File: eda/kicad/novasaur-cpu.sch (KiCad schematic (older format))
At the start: 29 parts, among them U14 27C020, U15 AS6C4008, U16 74F574, U17 74F163, U18 74F163, U19 74F541, U20 74F574, U21 74F574, U22 74F257, U23 74F574, U24 74F574, U25 74F574, U26 74F574, U27 74F244, U27 74F541

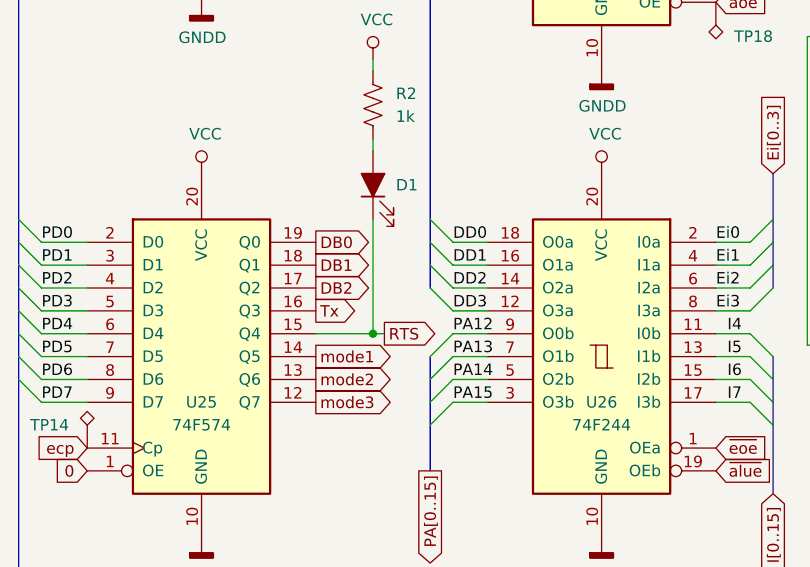
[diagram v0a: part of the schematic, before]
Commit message: build out, fix bugs Build out the initial HAL VM code to generate video timing. Not quite working yet, but lots of bugs fixed with assembler and code
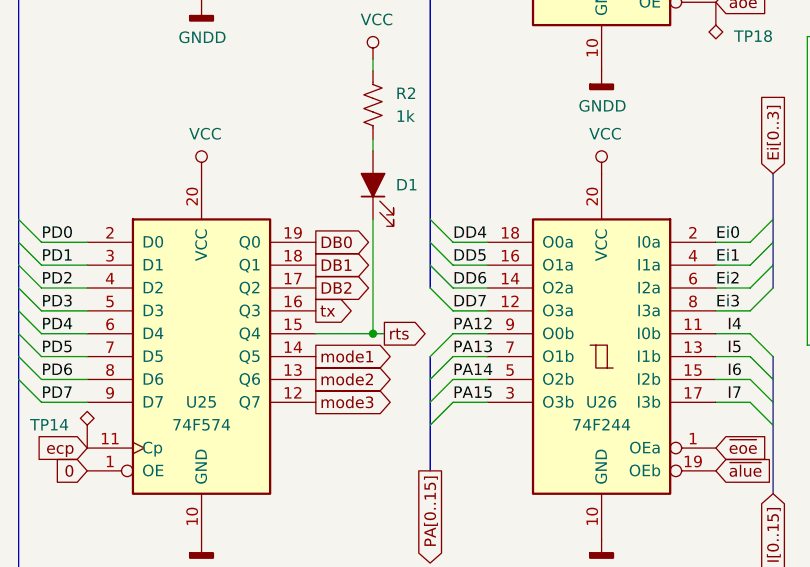
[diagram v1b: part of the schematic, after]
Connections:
- net DD0: no longer U27.18 (O0a)
- net DD1: no longer U27.16 (O1a)
- net DD2: no longer U27.14 (O2a)
- net DD3: no longer U27.12 (O3a)
- net DD4: now also U27.18 (O0a)
- net DD5: now also U27.16 (O1a)
- net DD6: now also U27.14 (O2a)
- net DD7: now also U27.12 (O3a)
- net RTS renamed rts
- net Tx renamed tx
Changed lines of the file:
@@
 Sheet 2 4
 Title "CPU"
-Date "2020-02-15"
+Date "2020-02-20"
 Rev "1.5"
 Comp ""
@@
 PA12
 Text Label 2650 6350 0    50   ~ 0
-DD3
+DD7
 Text Label 2650 6250 0    50   ~ 0
-DD2
+DD6
 Text Label 2650 6150 0    50   ~ 0
-DD1
+DD5
 Text Label 2650 6050 0    50   ~ 0
-DD0
+DD4
 Wire Wire Line
 	2650 6050 2800 6050
@@
 FD[0..7]
 Text GLabel 2050 6350 2    50   Output ~ 0
-Tx
+tx
 Text GLabel 2350 6450 2    50   Output ~ 0
-RTS
+rts
 Text GLabel 2050 6550 2    50   Output ~ 0
 mode1

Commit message: rename P reg to T
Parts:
- TP15: value ~POE -> ~TOE
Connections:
- net ~poe renamed ~toe
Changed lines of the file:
@@
 Sheet 2 4
 Title "CPU"
-Date "2020-03-08"
+Date "2020-03-29"
 Rev "1.6"
 Comp ""
@@
 PD[0..7]
 Text GLabel 4250 2400 0    50   Input ~ 0
-~poe
+~toe
 $Comp
 L 74xx:74LS574 U?
@@
 AR Path="/5DA1E9BD/5E39EF69" Ref="TP?"  Part="1"
 F 0 "TP15" H 4300 2550 50  0000 L CNN
-F 1 "~POE" H 4000 2550 50  0001 L CNN
+F 1 "~TOE" H 4000 2550 50  0001 L CNN
 F 2 "TestPoint:TestPoint_Pad_1.0x1.0mm" H 4450 2400 50  0001 C CNN
 F 3 "~" H 4450 2400 50  0001 C CNN

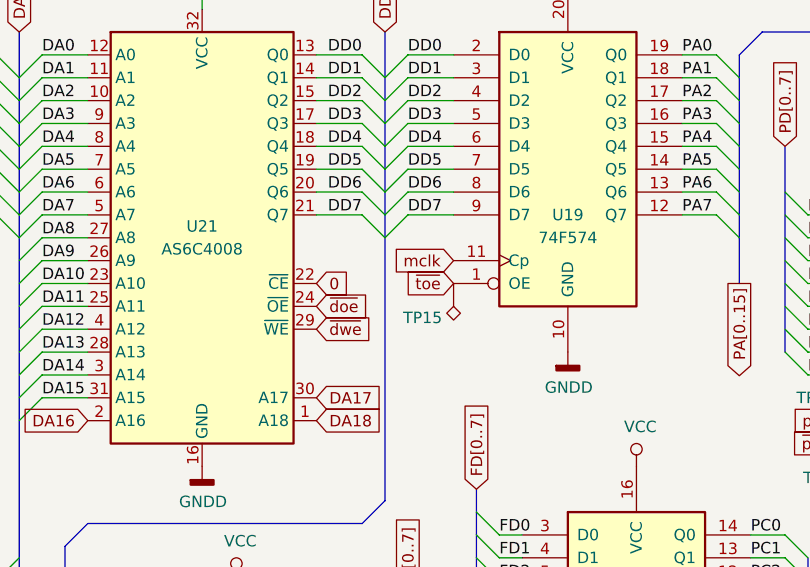
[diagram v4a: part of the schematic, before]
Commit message: add video headers
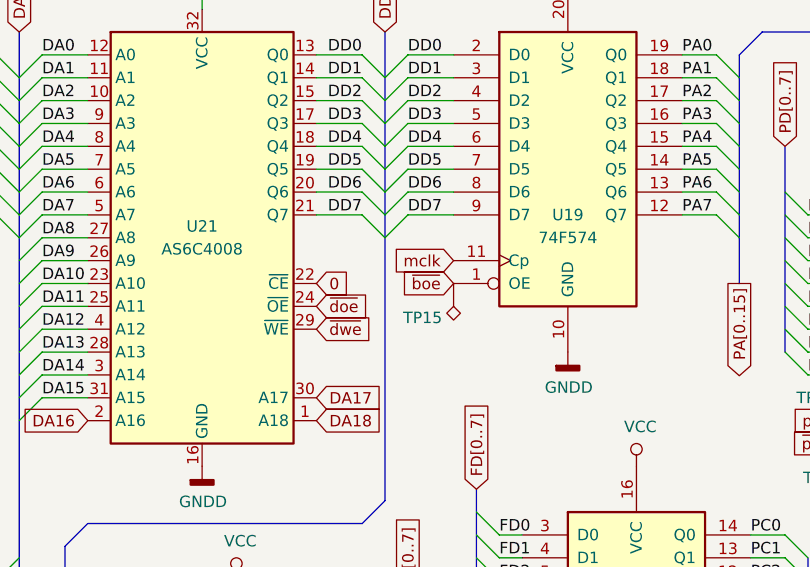
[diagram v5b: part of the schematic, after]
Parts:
- TP15: value ~TOE -> ~BOE
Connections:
- net ~toe renamed ~boe
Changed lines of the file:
@@
 encoding utf-8
 Sheet 2 4
-Title "CPU"
-Date "2020-03-29"
+Title "Novasaur Retrocomputer"
+Date "2020-03-31"
 Rev "1.6"
 Comp ""
@@
 PD[0..7]
 Text GLabel 4250 2400 0    50   Input ~ 0
-~toe
+~boe
 $Comp
 L 74xx:74LS574 U?
@@
 AR Path="/5DA1E9BD/5E39EF69" Ref="TP?"  Part="1"
 F 0 "TP15" H 4300 2550 50  0000 L CNN
-F 1 "~TOE" H 4000 2550 50  0001 L CNN
+F 1 "~BOE" H 4000 2550 50  0001 L CNN
 F 2 "TestPoint:TestPoint_Pad_1.0x1.0mm" H 4450 2400 50  0001 C CNN
 F 3 "~" H 4450 2400 50  0001 C CNN

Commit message: power sw + super caps
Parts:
- renumbered R2 to R1
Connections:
- net 0: no longer U15.22 (~CE)
- net VCC: no longer U15.32 (VCC)
- net I4 renamed C4
- net I5 renamed C5
- net I6 renamed C6
- net I7 renamed C7
- new net +BATT: U15.32 (VCC)
- new net ~dce: U15.22 (~CE)
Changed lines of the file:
@@
 Sheet 2 4
 Title "Novasaur Retrocomputer"
-Date "2020-03-31"
+Date "2020-05-02"
 Rev "1.6"
 Comp ""
@@
 Ei3
 Text Label 3850 6650 0    50   ~ 0
-I6
+C6
 Text Label 3850 6550 0    50   ~ 0
-I5
+C5
 Text Label 3850 6450 0    50   ~ 0
-I4
+C4
 Text Label 3850 6750 0    50   ~ 0
-I7
+C7
 Wire Wire Line
 	10000 5250 10150 5250
@@
 L power:VCC #PWR?
 U 1 1 5DAE3651
-P 8100 1200
+P 8100 1100
 AR Path="/5F6C0B36/5DAE3651" Ref="#PWR?"  Part="1"
 AR Path="/5DAA19D5/5DAE3651" Ref="#PWR0169"  Part="1"
 AR Path="/5DAA5CD8/5D99DA9F/5DAE3651" Ref="#PWR?"  Part="1"
 AR Path="/5DA1E9BA/5DAE3651" Ref="#PWR0129"  Part="1"
-F 0 "#PWR0129" H 8100 1050 50  0001 C CNN
-F 1 "VCC" H 8117 1373 50  0000 C CNN
-F 2 "" H 8100 1200 50  0001 C CNN
-F 3 "" H 8100 1200 50  0001 C CNN
-	1    8100 1200
+F 0 "#PWR0129" H 8100 950 50  0001 C CNN
+F 1 "VCC" H 8117 1273 50  0000 C CNN
+F 2 "" H 8100 1100 50  0001 C CNN
+F 3 "" H 8100 1100 50  0001 C CNN
+	1    8100 1100
 	1    0    0    -1
 $EndComp
@@
 $EndComp
 Wire Wire Line
-	3150 1200 3150 1100
-$Comp
-L power:VCC #PWR?
-U 1 1 5DAE363F
-P 3150 1100
-AR Path="/5F6C0B36/5DAE363F" Ref="#PWR?"  Part="1"
-AR Path="/5DAA19D5/5DAE363F" Ref="#PWR0166"  Part="1"
-AR Path="/5DAA5CD8/5D99DA9F/5DAE363F" Ref="#PWR?"  Part="1"
-AR Path="/5DA1E9BA/5DAE363F" Ref="#PWR0142"  Part="1"
-F 0 "#PWR0142" H 3150 950 50  0001 C CNN
-F 1 "VCC" H 3167 1273 50  0000 C CNN
-F 2 "" H 3150 1100 50  0001 C CNN
-F 3 "" H 3150 1100 50  0001 C CNN
-	1    3150 1100
-	1    0    0    -1
-$EndComp
-Wire Wire Line
 	2450 1400 2650 1400
 Wire Wire Line
@@
 	2450 2900 2650 2900
 Text GLabel 4050 7150 3    50   Input ~ 0
-I[0..15]
+C[0..15]
 Text GLabel 3950 1300 1    50   Input ~ 0
 DD[0..7]
@@
 DA17
 Text GLabel 3650 2400 2    50   Input ~ 0
-0
+~dce
 Text GLabel 3650 2600 2    50   Input ~ 0
 ~dwe
@@
 AR Path="/5DA1E9BA/5EE6CB39" Ref="D1"  Part="1"
 AR Path="/5EE6CB39" Ref="D?"  Part="1"
-F 0 "D1" V 2300 5700 50  0000 R CNN
+F 0 "D1" V 2300 6000 50  0000 R CNN
 F 1 "4300H1LC" V 2248 5683 50  0001 R CNN
 F 2 "LED_THT:LED_D5.0mm_Horizontal_O1.27mm_Z3.0mm" H 2300 5800 50  0001 C CNN
@@
 AR Path="/5DAA19D5/5EE6CB33" Ref="R?"  Part="1"
 AR Path="/5DAA5CD8/5D99DA9F/5EE6CB33" Ref="R?"  Part="1"
-AR Path="/5DA1E9BA/5EE6CB33" Ref="R2"  Part="1"
+AR Path="/5DA1E9BA/5EE6CB33" Ref="R1"  Part="1"
 AR Path="/5EE6CB33" Ref="R?"  Part="1"
-F 0 "R2" H 2400 5500 50  0000 L CNN
-F 1 "1k" H 2400 5400 50  0000 L CNN
+F 0 "R1" H 2100 5500 50  0000 L CNN
+F 1 "1k" H 2100 5400 50  0000 L CNN
 F 2 "Resistor_THT:R_Axial_DIN0204_L3.6mm_D1.6mm_P7.62mm_Horizontal" V 2340 5440 50  0001 C CNN
 F 3 "~" H 2300 5450 50  0001 C CNN
@@
 Wire Wire Line
 	2300 5650 2300 5600
+$Comp
+L power:+BATT #PWR0142
+U 1 1 5EC0EA23
+P 3150 1100
+F 0 "#PWR0142" H 3150 950 50  0001 C CNN
+F 1 "+BATT" H 3165 1273 50  0000 C CNN
+F 2 "" H 3150 1100 50  0001 C CNN
+F 3 "" H 3150 1100 50  0001 C CNN
+	1    3150 1100
+	1    0    0    -1
+$EndComp
+Wire Wire Line
+	3150 1200 3150 1100
+Wire Wire Line
+	8100 1200 8100 1100
 Wire Bus Line
 	4350 3300 4350 3700

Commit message: update serial
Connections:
- net Ei0 renamed rx
- net Ei1 renamed cts
- net Ei2 renamed ps2clk
- net Ei3 renamed ps2rx
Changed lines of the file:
@@
 encoding utf-8
 Sheet 2 4
-Title "Novasaur Retrocomputer"
-Date "2020-05-02"
+Title "Central Processing Unit"
+Date "2020-05-24"
 Rev "1.6"
 Comp ""
@@
 Wire Wire Line
 	3800 6450 3950 6450
-Wire Wire Line
-	3800 6350 3950 6350
-Wire Wire Line
-	3800 6150 3950 6150
-Wire Wire Line
-	3800 6050 3950 6050
 Entry Wire Line
 	3950 6750 4050 6850
@@
 Entry Wire Line
 	3950 6450 4050 6550
-Entry Wire Line
-	3950 6050 4050 5950
-Entry Wire Line
-	3950 6150 4050 6050
-Entry Wire Line
-	3950 6250 4050 6150
-Entry Wire Line
-	3950 6350 4050 6250
 Text Label 2650 6750 0    50   ~ 0
 PA15
@@
 Entry Wire Line
 	2550 6850 2650 6750
-Wire Wire Line
-	3950 6250 3800 6250
-Text Label 3800 6050 0    50   ~ 0
-Ei0
-Text Label 3800 6150 0    50   ~ 0
-Ei1
-Text Label 3800 6250 0    50   ~ 0
-Ei2
-Text Label 3800 6350 0    50   ~ 0
-Ei3
 Text Label 3850 6650 0    50   ~ 0
 C6
@@
 Text GLabel 4350 5600 1    50   Input ~ 0
 FD[0..7]
-Text GLabel 4050 5750 1    50   Input ~ 0
-Ei[0..3]
 Wire Wire Line
 	8900 4850 8900 4650
@@
 Wire Wire Line
 	8100 1200 8100 1100
+Text GLabel 3800 6050 2    50   Input ~ 0
+rx
+Text GLabel 3800 6150 2    50   Input ~ 0
+cts
+Text GLabel 3800 6250 2    50   Input ~ 0
+ps2clk
+Text GLabel 3800 6350 2    50   Input ~ 0
+ps2rx
 Wire Bus Line
 	4350 3300 4350 3700
@@
 	2550 6550 2550 7050
 Wire Bus Line
-	4050 5750 4050 6250
-Wire Bus Line
 	4050 6550 4050 7150

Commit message: checkin work in progress on video timing
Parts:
- D1: value 4300H1LC -> LTL-10223W
- R1: value 1k -> 330
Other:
- moved on the sheet: TP19, TP20, U16
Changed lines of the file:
@@
 Sheet 2 4
 Title "Central Processing Unit"
-Date "2020-05-24"
+Date "2020-07-04"
 Rev "1.6"
 Comp ""
@@
 	1    0    0    -1
 $EndComp
-Entry Bus Bus
-	7250 1300 7350 1400
 Wire Wire Line
 	7450 1400 7700 1400
@@
 	7450 1900 7700 1900
 Entry Wire Line
+	7250 1400 7350 1500
+Entry Wire Line
+	7250 1500 7350 1600
+Entry Wire Line
+	7250 1600 7350 1700
+Entry Wire Line
+	7250 1700 7350 1800
+Entry Wire Line
+	7250 1800 7350 1900
+Entry Wire Line
+	7250 1900 7350 2000
+Entry Wire Line
+	7250 2000 7350 2100
+Entry Wire Line
 	7250 2100 7350 2200
-Entry Wire Line
-	7250 2200 7350 2300
-Entry Wire Line
-	7250 2300 7350 2400
-Entry Wire Line
-	7250 2400 7350 2500
-Entry Wire Line
-	7250 2500 7350 2600
-Entry Wire Line
-	7250 2600 7350 2700
-Entry Wire Line
-	7250 2700 7350 2800
-Entry Wire Line
-	7250 2800 7350 2900
 $Comp
 L 74xx:74LS574 U?
 U 1 1 5DAE33CE
-P 6500 2600
+P 6500 1900
 AR Path="/5F6C0B36/5DAE33CE" Ref="U?"  Part="1"
 AR Path="/5DAA19D5/5DAE33CE" Ref="U20"  Part="1"
 AR Path="/5DAA5CD8/5D99DA9F/5DAE33CE" Ref="U?"  Part="1"
 AR Path="/5DA1E9BA/5DAE33CE" Ref="U16"  Part="1"
-F 0 "U16" H 6500 2400 50  0000 C CNN
-F 1 "74F574" H 6500 2300 50  0000 C CNN
-F 2 "Package_DIP:DIP-20_W7.62mm_LongPads" H 6500 2600 50  0001 C CNN
-F 3 "http://www.ti.com/lit/gpn/sn74LS574" H 6500 2600 50  0001 C CNN
-	1    6500 2600
-	1    0    0    -1
-$EndComp
-Text Label 7100 2100 0    50   ~ 0
+F 0 "U16" H 6500 1700 50  0000 C CNN
+F 1 "74F574" H 6500 1600 50  0000 C CNN
+F 2 "Package_DIP:DIP-20_W7.62mm_LongPads" H 6500 1900 50  0001 C CNN
+F 3 "http://www.ti.com/lit/gpn/sn74LS574" H 6500 1900 50  0001 C CNN
+	1    6500 1900
+	1    0    0    -1
+$EndComp
+Text Label 7100 1400 0    50   ~ 0
 PA8
-Text Label 7100 2200 0    50   ~ 0
+Text Label 7100 1500 0    50   ~ 0
 PA9
-Text Label 7050 2300 0    50   ~ 0
+Text Label 7050 1600 0    50   ~ 0
 PA10
-Text Label 7050 2400 0    50   ~ 0
+Text Label 7050 1700 0    50   ~ 0
 PA11
-Text Label 7050 2500 0    50   ~ 0
+Text Label 7050 1800 0    50   ~ 0
 PA12
-Text Label 7050 2600 0    50   ~ 0
+Text Label 7050 1900 0    50   ~ 0
 PA13
-Text Label 7050 2700 0    50   ~ 0
+Text Label 7050 2000 0    50   ~ 0
 PA14
-Text Label 7050 2800 0    50   ~ 0
+Text Label 7050 2100 0    50   ~ 0
 PA15
 $Comp
 L power:GNDD #PWR?
 U 1 1 5DAE35F1
-P 6500 3400
+P 6500 2700
 AR Path="/5F6C0B36/5DAE35F1" Ref="#PWR?"  Part="1"
 AR Path="/5DAA19D5/5DAE35F1" Ref="#PWR0158"  Part="1"
 AR Path="/5DAA5CD8/5D99DA9F/5DAE35F1" Ref="#PWR?"  Part="1"
 AR Path="/5DA1E9BA/5DAE35F1" Ref="#PWR0120"  Part="1"
-F 0 "#PWR0120" H 6500 3150 50  0001 C CNN
-F 1 "GNDD" H 6504 3245 50  0000 C CNN
-F 2 "" H 6500 3400 50  0001 C CNN
-F 3 "" H 6500 3400 50  0001 C CNN
-	1    6500 3400
+F 0 "#PWR0120" H 6500 2450 50  0001 C CNN
+F 1 "GNDD" H 6504 2545 50  0000 C CNN
+F 2 "" H 6500 2700 50  0001 C CNN
+F 3 "" H 6500 2700 50  0001 C CNN
+	1    6500 2700
 	1    0    0    -1
 $EndComp
@@
 L power:VCC #PWR?
 U 1 1 5DAE367B
-P 6500 1800
+P 6500 1100
 AR Path="/5F6C0B36/5DAE367B" Ref="#PWR?"  Part="1"
 AR Path="/5DAA19D5/5DAE367B" Ref="#PWR0176"  Part="1"
 AR Path="/5DAA5CD8/5D99DA9F/5DAE367B" Ref="#PWR?"  Part="1"
 AR Path="/5DA1E9BA/5DAE367B" Ref="#PWR0132"  Part="1"
-F 0 "#PWR0132" H 6500 1650 50  0001 C CNN
-F 1 "VCC" H 6517 1973 50  0000 C CNN
-F 2 "" H 6500 1800 50  0001 C CNN
-F 3 "" H 6500 1800 50  0001 C CNN
-	1    6500 1800
+F 0 "#PWR0132" H 6500 950 50  0001 C CNN
+F 1 "VCC" H 6517 1273 50  0000 C CNN
+F 2 "" H 6500 1100 50  0001 C CNN
+F 3 "" H 6500 1100 50  0001 C CNN
+	1    6500 1100
 	1    0    0    -1
 $EndComp
@@
 Text GLabel 6100 5350 0    50   Input ~ 0
 alu
-Text GLabel 5700 1800 1    50   Input ~ 0
-PD[0..7]
 Text GLabel 4250 2400 0    50   Input ~ 0
 ~boe
@@
 	1    0    0    -1
 $EndComp
-Entry Bus Bus
-	5500 1400 5600 1300
 $Comp
 L novasaur-rescue:628128_DIP32_SSOP32-Memory_RAM U15
@@
 Text GLabel 4050 7150 3    50   Input ~ 0
 C[0..15]
-Text GLabel 3950 1300 1    50   Input ~ 0
-DD[0..7]
 $Comp
 L 74xx:74LS244 U?
@@
 	1    0    0    -1
 $EndComp
-Text GLabel 5500 2400 3    50   Output ~ 0
+Text GLabel 7350 1350 1    50   Input ~ 0
 PA[0..15]
 Text Label 2450 2900 0    50   ~ 0
@@
 Text Label 850  1400 0    50   ~ 0
 PD0
-Text Label 5800 2800 0    50   ~ 0
+Text Label 5800 2100 0    50   ~ 0
 PD7
-Text Label 5800 2700 0    50   ~ 0
+Text Label 5800 2000 0    50   ~ 0
 PD6
-Text Label 5800 2600 0    50   ~ 0
+Text Label 5800 1900 0    50   ~ 0
 PD5
-Text Label 5800 2500 0    50   ~ 0
+Text Label 5800 1800 0    50   ~ 0
 PD4
-Text Label 5800 2400 0    50   ~ 0
+Text Label 5800 1700 0    50   ~ 0
 PD3
-Text Label 5800 2300 0    50   ~ 0
+Text Label 5800 1600 0    50   ~ 0
 PD2
-Text Label 5800 2200 0    50   ~ 0
+Text Label 5800 1500 0    50   ~ 0
 PD1
-Text Label 5800 2100 0    50   ~ 0
+Text Label 5800 1400 0    50   ~ 0
 PD0
-Text GLabel 6000 3000 0    50   Input ~ 0
+Text GLabel 6000 2300 0    50   Input ~ 0
 pgcp
-Text GLabel 6000 3100 0    50   Input ~ 0
+Text GLabel 6000 2400 0    50   Input ~ 0
 ~pgoe
 Text Label 4050 2100 0    50   ~ 0
@@
 Text Label 7100 4450 0    50   ~ 0
 PA0
-Text GLabel 2350 1300 1    50   Input ~ 0
-DA[0..15]
 $Comp
 L power:GNDD #PWR?
@@
 $EndComp
 Entry Wire Line
-	5800 2800 5700 2700
-Entry Wire Line
-	5800 2700 5700 2600
-Entry Wire Line
-	5800 2600 5700 2500
-Entry Wire Line
-	5800 2500 5700 2400
-Entry Wire Line
-	5800 2400 5700 2300
-Entry Wire Line
-	5800 2300 5700 2200
-Entry Wire Line
-	5800 2200 5700 2100
-Entry Wire Line
 	5800 2100 5700 2000
+Entry Wire Line
+	5800 2000 5700 1900
+Entry Wire Line
+	5800 1900 5700 1800
+Entry Wire Line
+	5800 1800 5700 1700
+Entry Wire Line
+	5800 1700 5700 1600
+Entry Wire Line
+	5800 1600 5700 1500
+Entry Wire Line
+	5800 1500 5700 1400
+Entry Wire Line
+	5800 1400 5700 1300
 Entry Wire Line
 	750  2000 850  2100
@@
 FD[0..7]
 Wire Wire Line
-	7000 2800 7250 2800
-Wire Wire Line
-	7000 2700 7250 2700
-Wire Wire Line
-	7000 2600 7250 2600
-Wire Wire Line
-	7000 2500 7250 2500
-Wire Wire Line
-	7000 2400 7250 2400
-Wire Wire Line
-	7000 2300 7250 2300
-Wire Wire Line
-	7000 2200 7250 2200
-Wire Wire Line
 	7000 2100 7250 2100
+Wire Wire Line
+	7000 2000 7250 2000
+Wire Wire Line
+	7000 1900 7250 1900
+Wire Wire Line
+	7000 1800 7250 1800
+Wire Wire Line
+	7000 1700 7250 1700
+Wire Wire Line
+	7000 1600 7250 1600
+Wire Wire Line
+	7000 1500 7250 1500
+Wire Wire Line
+	7000 1400 7250 1400
 Wire Wire Line
 	4450 3800 4550 3800
@@
 	850  2100 1050 2100
 Wire Wire Line
+	5800 1400 6000 1400
+Wire Wire Line
+	5800 1500 6000 1500
+Wire Wire Line
+	5800 1600 6000 1600
+Wire Wire Line
+	5800 1700 6000 1700
+Wire Wire Line
+	5800 1800 6000 1800
+Wire Wire Line
+	5800 1900 6000 1900
+Wire Wire Line
+	5800 2000 6000 2000
+Wire Wire Line
 	5800 2100 6000 2100
-Wire Wire Line
-	5800 2200 6000 2200
-Wire Wire Line
-	5800 2300 6000 2300
-Wire Wire Line
-	5800 2400 6000 2400
-Wire Wire Line
-	5800 2500 6000 2500
-Wire Wire Line
-	5800 2600 6000 2600
-Wire Wire Line
-	5800 2700 6000 2700
-Wire Wire Line
-	5800 2800 6000 2800
 Wire Wire Line
 	5900 4450 6100 4450
@@
 	5900 6450 10150 6450
 Wire Bus Line
-	5600 1300 7250 1300
-Wire Bus Line
 	850  7700 5700 7700
 Wire Bus Line
 	5800 6550 5800 7600
-Wire Bus Line
-	850  800  10150 800
 $Comp
 L 74xx:74LS541 U?
@@
 L Connector:TestPoint_Alt TP?
 U 1 1 5DF36352
-P 6000 3000
+P 6000 2300
 AR Path="/5DF36352" Ref="TP?"  Part="1"
 AR Path="/5DA1E9BA/5DF36352" Ref="TP19"  Part="1"
-F 0 "TP19" H 5750 3100 50  0000 L CNN
-F 1 "PGCP" H 5750 3150 50  0001 L CNN
-F 2 "TestPoint:TestPoint_Pad_1.0x1.0mm" H 6200 3000 50  0001 C CNN
-F 3 "~" H 6200 3000 50  0001 C CNN
-	1    6000 3000
+F 0 "TP19" H 5750 2400 50  0000 L CNN
+F 1 "PGCP" H 5750 2450 50  0001 L CNN
+F 2 "TestPoint:TestPoint_Pad_1.0x1.0mm" H 6200 2300 50  0001 C CNN
+F 3 "~" H 6200 2300 50  0001 C CNN
+	1    6000 2300
 	1    0    0    -1
 $EndComp
@@
 L Connector:TestPoint_Alt TP?
 U 1 1 5E39EF6F
-P 6000 3100
+P 6000 2400
 AR Path="/5E39EF6F" Ref="TP?"  Part="1"
 AR Path="/5DA1E9BA/5E39EF6F" Ref="TP20"  Part="1"
 AR Path="/5DA1E9BD/5E39EF6F" Ref="TP?"  Part="1"
-F 0 "TP20" H 6050 3250 50  0000 L CNN
-F 1 "~PGOE" H 5750 3250 50  0001 L CNN
-F 2 "TestPoint:TestPoint_Pad_1.0x1.0mm" H 6200 3100 50  0001 C CNN
-F 3 "~" H 6200 3100 50  0001 C CNN
-	1    6000 3100
+F 0 "TP20" H 6050 2550 50  0000 L CNN
+F 1 "~PGOE" H 5750 2550 50  0001 L CNN
+F 2 "TestPoint:TestPoint_Pad_1.0x1.0mm" H 6200 2400 50  0001 C CNN
+F 3 "~" H 6200 2400 50  0001 C CNN
+	1    6000 2400
 	-1   0    0    1
 $EndComp
@@
 AR Path="/5EE6CB39" Ref="D?"  Part="1"
 F 0 "D1" V 2300 6000 50  0000 R CNN
-F 1 "4300H1LC" V 2248 5683 50  0001 R CNN
+F 1 "LTL-10223W" V 2248 5683 50  0001 R CNN
 F 2 "LED_THT:LED_D5.0mm_Horizontal_O1.27mm_Z3.0mm" H 2300 5800 50  0001 C CNN
 F 3 "~" H 2300 5800 50  0001 C CNN
@@
 AR Path="/5EE6CB33" Ref="R?"  Part="1"
 F 0 "R1" H 2100 5500 50  0000 L CNN
-F 1 "1k" H 2100 5400 50  0000 L CNN
+F 1 "330" H 2050 5400 50  0000 L CNN
 F 2 "Resistor_THT:R_Axial_DIN0204_L3.6mm_D1.6mm_P7.62mm_Horizontal" V 2340 5440 50  0001 C CNN
 F 3 "~" H 2300 5450 50  0001 C CNN
@@
 Text GLabel 3800 6350 2    50   Input ~ 0
 ps2rx
+Entry Bus Bus
+	5700 900  5800 800
+Entry Bus Bus
+	7250 3100 7350 3000
+Entry Bus Bus
+	5500 3000 5600 3100
+Wire Bus Line
+	7250 3100 5600 3100
+Text GLabel 2350 1300 1    50   Input ~ 0
+DA[0..15]
+Text GLabel 3950 1300 1    50   BiDi ~ 0
+DD[0..7]
+Wire Bus Line
+	850  800  10150 800
 Wire Bus Line
 	4350 3300 4350 3700
@@
 	3950 1300 3950 3350
 Wire Bus Line
-	5700 1800 5700 2700
+	5500 1500 5500 3000
+Wire Bus Line
+	5700 900  5700 2000
 Wire Bus Line
 	8800 1500 8800 2500
@@
 	2550 3550 2550 6250
 Wire Bus Line
-	5500 1400 5500 2400
-Wire Bus Line
 	10250 2850 10250 6350
 Wire Bus Line
 	2350 1300 2350 4300
 Wire Bus Line
-	7350 1400 7350 5350
+	7350 1350 7350 5350
 Wire Bus Line
 	750  900  750  7600
